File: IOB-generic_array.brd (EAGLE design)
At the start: 106.7 x 104.1 mm, 79 parts

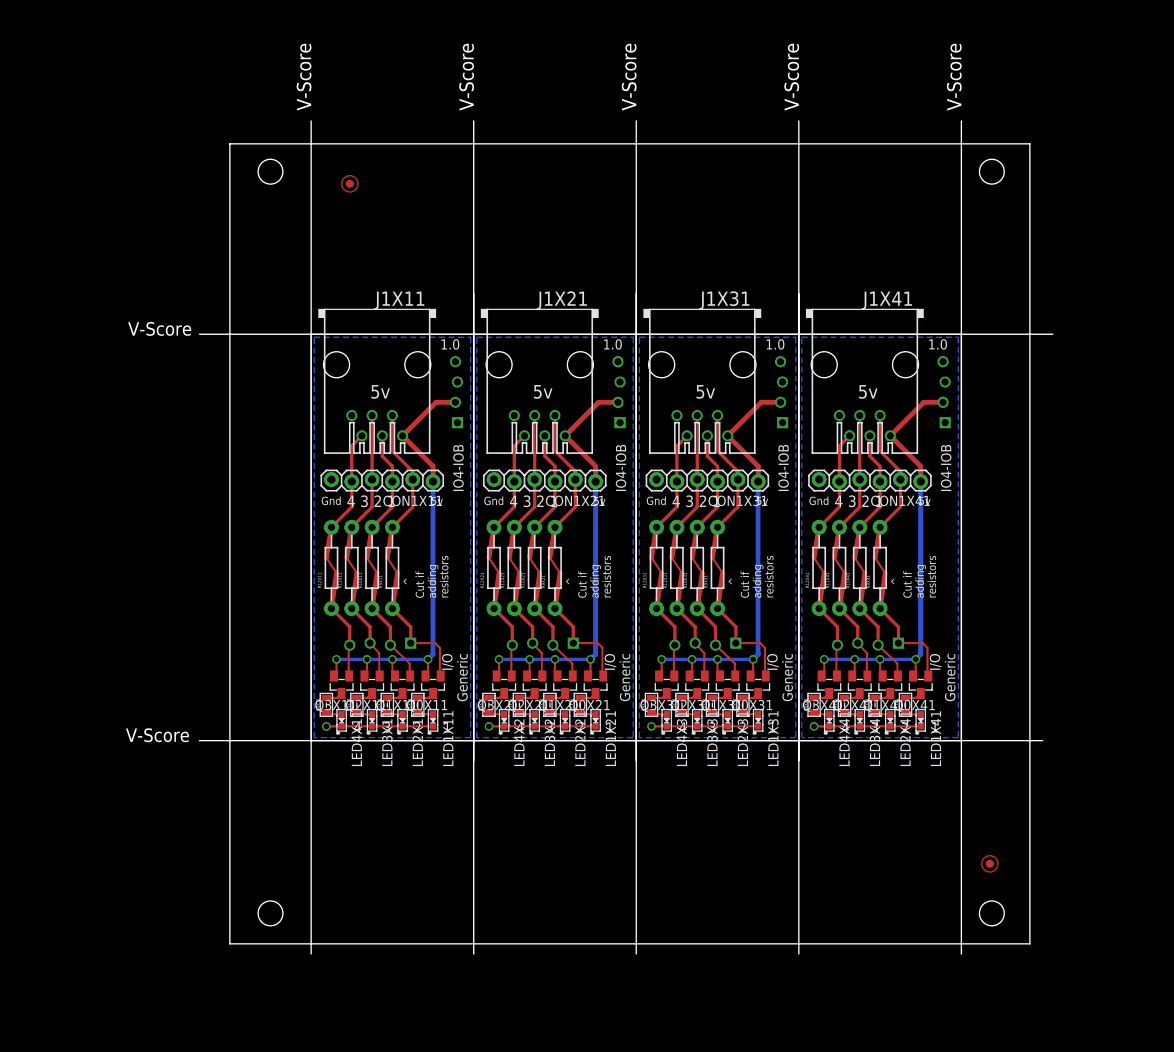
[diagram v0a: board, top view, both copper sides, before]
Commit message: generated new array
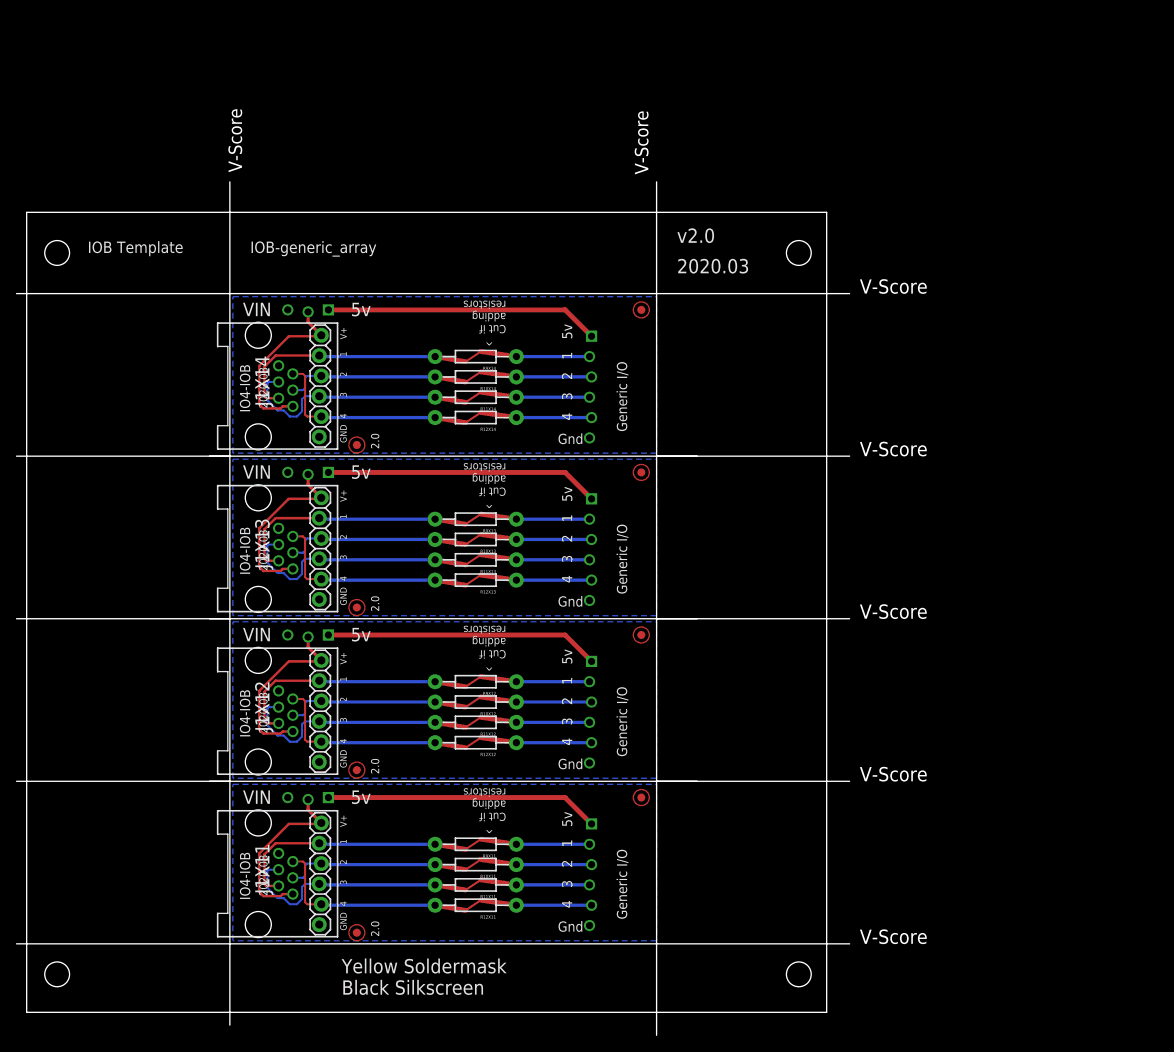
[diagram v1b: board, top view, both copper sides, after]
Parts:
- removed CON1X11, CON1X21, CON1X31, CON1X41: (no value), SPCoast:1X06_LOCK
- removed FID1, FID3: (no value), SPCoast:FIDUCIAL_1MM
- removed IOBX21, IOBX31, IOBX41: (no value), SPCoast:IO4-IOB
- removed J1X21, J1X31, J1X41: (no value), SPCoast:RJ25-PANEL
- removed LED1X11, LED1X21, LED1X31, LED1X41, LED2X11, LED2X21, LED2X31, LED2X41, LED3X11, LED3X21, LED3X31, LED3X41, LED4X11, LED4X21, LED4X31, LED4X41: (no value), SPCoast:0603-LED
- removed Q0X11, Q0X21, Q0X31, Q0X41, Q1X11, Q1X21, Q1X31, Q1X41, Q2X11, Q2X21, Q2X31, Q2X41, Q3X11, Q3X21, Q3X31, Q3X41: (no value), SPCoast:SOT23
- removed R10X21, R10X31, R10X41, R11X21, R11X31, R11X41, R12X21, R12X31, R12X41, R9X21, R9X31, R9X41: (no value), SPCoast:AXIAL-0.4-RES
- removed R1X11, R1X21, R1X31, R1X41, R2X11, R2X21, R2X31, R2X41, R3X11, R3X21, R3X31, R3X41, R4X11, R4X21, R4X31, R4X41: (no value), SPCoast:0805-RES
- removed VINX1: (no value), SPCoast:BOARD-DINRAIL-3.17IN-4X-IOB
- added FID1X11, FID1X12, FID1X13, FID1X14, FID2X11, FID2X12, FID2X13, FID2X14: (no value), SPCoast:FIDUCIAL_1MM
- added IOBX12, IOBX13, IOBX14: (no value), SPCoast:IO4-IOB
- added J1X12, J1X13, J1X14: (no value), SPCoast:RJ24-INVERTED-PINS
- added R10X12, R10X13, R10X14, R11X12, R11X13, R11X14, R12X12, R12X13, R12X14, R9X12, R9X13, R9X14: (no value), SPCoast:AXIAL-0.4-RES
- added R12X1: (no value), SPCoast:BOARD-DINRAIL-3.17IN-H4X-IOB
- J1X11: device SPCoast:RJ25-PANEL -> SPCoast:RJ24-INVERTED-PINS
- moved IOBX11 76.9 mm to (0.00, 0.00), turned to 0 degrees
- moved J1X11 64.6 mm to (7.37, 8.76), turned to 90 degrees
- moved R12X11 45.9 mm to (30.7, 4.83), turned to 180 degrees
- moved R11X11 42.5 mm to (30.7, 7.37), turned to 180 degrees
- moved R10X11 39.3 mm to (30.7, 9.91), turned to 180 degrees
- moved R9X11 36.1 mm to (30.7, 12.4), turned to 180 degrees
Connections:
- removed net !IO1X21: CON1X21.2, J1X21.2, R9X21.P$2
- removed net !IO1X31: CON1X31.2, J1X31.2, R9X31.P$2
- removed net !IO1X41: CON1X41.2, J1X41.2, R9X41.P$2
- removed net !IO2X21: CON1X21.3, J1X21.3, R10X21.P$2
- removed net !IO2X31: CON1X31.3, J1X31.3, R10X31.P$2
- removed net !IO2X41: CON1X41.3, J1X41.3, R10X41.P$2
- removed net !IO3X21: CON1X21.4, J1X21.4, R11X21.P$2
- removed net !IO3X31: CON1X31.4, J1X31.4, R11X31.P$2
- removed net !IO3X41: CON1X41.4, J1X41.4, R11X41.P$2
- removed net !IO4X21: CON1X21.5, J1X21.5, R12X21.P$2
- removed net !IO4X31: CON1X31.5, J1X31.5, R12X31.P$2
- removed net !IO4X41: CON1X41.5, J1X41.5, R12X41.P$2
- removed net GNDX21: CON1X21.6, IOBX21.G@1, IOBX21.G@2, J1X21.6, LED1X21.C, LED2X21.C, LED3X21.C, LED4X21.C
- removed net GNDX31: CON1X31.6, IOBX31.G@1, IOBX31.G@2, J1X31.6, LED1X31.C, LED2X31.C, LED3X31.C, LED4X31.C
- removed net GNDX41: CON1X41.6, IOBX41.G@1, IOBX41.G@2, J1X41.6, LED1X41.C, LED2X41.C, LED3X41.C, LED4X41.C
- removed net N$11X11: Q0X11.3, R1X11.2
- removed net N$11X21: Q0X21.3, R1X21.2
- removed net N$11X31: Q0X31.3, R1X31.2
- removed net N$11X41: Q0X41.3, R1X41.2
- removed net N$2X11: LED1X11.A, R1X11.1
- removed net N$2X21: LED1X21.A, R1X21.1
- removed net N$2X31: LED1X31.A, R1X31.1
- removed net N$2X41: LED1X41.A, R1X41.1
- removed net N$30X11: Q1X11.3, R2X11.2
- removed net N$30X21: Q1X21.3, R2X21.2
- removed net N$30X31: Q1X31.3, R2X31.2
- removed net N$30X41: Q1X41.3, R2X41.2
- removed net N$31X11: Q2X11.3, R3X11.2
- removed net N$31X21: Q2X21.3, R3X21.2
- removed net N$31X31: Q2X31.3, R3X31.2
- removed net N$31X41: Q2X41.3, R3X41.2
- removed net N$32X11: Q3X11.3, R4X11.2
- removed net N$32X21: Q3X21.3, R4X21.2
- removed net N$32X31: Q3X31.3, R4X31.2
- removed net N$32X41: Q3X41.3, R4X41.2
- removed net N$3X11: LED2X11.A, R2X11.1
- removed net N$3X21: LED2X21.A, R2X21.1
- removed net N$3X31: LED2X31.A, R2X31.1
- removed net N$3X41: LED2X41.A, R2X41.1
- removed net N$4X11: LED3X11.A, R3X11.1
- removed net N$4X21: LED3X21.A, R3X21.1
- removed net N$4X31: LED3X31.A, R3X31.1
- removed net N$4X41: LED3X41.A, R3X41.1
- removed net N$5X11: LED4X11.A, R4X11.1
- removed net N$5X21: LED4X21.A, R4X21.1
- removed net N$5X31: LED4X31.A, R4X31.1
- removed net N$5X41: LED4X41.A, R4X41.1
- removed net P1X21: IOBX21.P1, Q0X21.1, R9X21.P$1
- removed net P1X31: IOBX31.P1, Q0X31.1, R9X31.P$1
- removed net P1X41: IOBX41.P1, Q0X41.1, R9X41.P$1
- removed net P2X21: IOBX21.P2, Q1X21.1, R10X21.P$1
- removed net P2X31: IOBX31.P2, Q1X31.1, R10X31.P$1
- removed net P2X41: IOBX41.P2, Q1X41.1, R10X41.P$1
- removed net P3X21: IOBX21.P3, Q2X21.1, R11X21.P$1
- removed net P3X31: IOBX31.P3, Q2X31.1, R11X31.P$1
- removed net P3X41: IOBX41.P3, Q2X41.1, R11X41.P$1
- removed net P4X21: IOBX21.P4, Q3X21.1, R12X21.P$1
- removed net P4X31: IOBX31.P4, Q3X31.1, R12X31.P$1
- removed net P4X41: IOBX41.P4, Q3X41.1, R12X41.P$1
- removed net VCCIOX21: IOBX21.V+
- removed net VCCIOX31: IOBX31.V+
- removed net VCCIOX41: IOBX41.V+
- removed net VCCX21: CON1X21.1, IOBX21.V5, J1X21.1, Q0X21.2, Q1X21.2, Q2X21.2, Q3X21.2
- removed net VCCX31: CON1X31.1, IOBX31.V5, J1X31.1, Q0X31.2, Q1X31.2, Q2X31.2, Q3X31.2
- removed net VCCX41: CON1X41.1, IOBX41.V5, J1X41.1, Q0X41.2, Q1X41.2, Q2X41.2, Q3X41.2
- new net !IO1X12: J1X12.2, J1X12.2@1, R9X12.P$2
- new net !IO1X13: J1X13.2, J1X13.2@1, R9X13.P$2
- new net !IO1X14: J1X14.2, J1X14.2@1, R9X14.P$2
- new net !IO2X12: J1X12.3, J1X12.3@1, R10X12.P$2
- new net !IO2X13: J1X13.3, J1X13.3@1, R10X13.P$2
- new net !IO2X14: J1X14.3, J1X14.3@1, R10X14.P$2
- new net !IO3X12: J1X12.4, J1X12.4@1, R11X12.P$2
- new net !IO3X13: J1X13.4, J1X13.4@1, R11X13.P$2
- new net !IO3X14: J1X14.4, J1X14.4@1, R11X14.P$2
- new net !IO4X12: J1X12.5, J1X12.5@1, R12X12.P$2
- new net !IO4X13: J1X13.5, J1X13.5@1, R12X13.P$2
- new net !IO4X14: J1X14.5, J1X14.5@1, R12X14.P$2
- new net GNDX12: IOBX12.G@3, J1X12.6, J1X12.6@1
- new net GNDX13: IOBX13.G@3, J1X13.6, J1X13.6@1
- new net GNDX14: IOBX14.G@3, J1X14.6, J1X14.6@1
- new net P1X12: IOBX12.P1, R9X12.P$1
- new net P1X13: IOBX13.P1, R9X13.P$1
- new net P1X14: IOBX14.P1, R9X14.P$1
- new net P2X12: IOBX12.P2, R10X12.P$1
- new net P2X13: IOBX13.P2, R10X13.P$1
- new net P2X14: IOBX14.P2, R10X14.P$1
- new net P3X12: IOBX12.P3, R11X12.P$1
- new net P3X13: IOBX13.P3, R11X13.P$1
- new net P3X14: IOBX14.P3, R11X14.P$1
- new net P4X12: IOBX12.P4, R12X12.P$1
- new net P4X13: IOBX13.P4, R12X13.P$1
- new net P4X14: IOBX14.P4, R12X14.P$1
- new net VCCIOX12: IOBX12.V+
- new net VCCIOX13: IOBX13.V+
- new net VCCIOX14: IOBX14.V+
- new net VCCX12: IOBX12.V5, IOBX12.V5@1
- new net VCCX13: IOBX13.V5, IOBX13.V5@1
- new net VCCX14: IOBX14.V5, IOBX14.V5@1
- new net VOUTX11: IOBX11.VOUT, J1X11.1, J1X11.1@1
- new net VOUTX12: IOBX12.VOUT, J1X12.1, J1X12.1@1
- new net VOUTX13: IOBX13.VOUT, J1X13.1, J1X13.1@1
- new net VOUTX14: IOBX14.VOUT, J1X14.1, J1X14.1@1
- net !IO1X11: now also J1X11.2@1; no longer CON1X11.2
- net !IO2X11: now also J1X11.3@1; no longer CON1X11.3
- net !IO3X11: now also J1X11.4@1; no longer CON1X11.4
- net !IO4X11: now also J1X11.5@1; no longer CON1X11.5
- net GNDX11: now also IOBX11.G@3, J1X11.6@1; no longer CON1X11.6, IOBX11.G@1, IOBX11.G@2, LED1X11.C, LED2X11.C, LED3X11.C, LED4X11.C
- net P1X11: no longer Q0X11.1
- net P2X11: no longer Q1X11.1
- net P3X11: no longer Q2X11.1
- net P4X11: no longer Q3X11.1
- net VCCX11: now also IOBX11.V5@1; no longer CON1X11.1, J1X11.1, Q0X11.2, Q1X11.2, Q2X11.2, Q3X11.2
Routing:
- net VCCX31: track 58.7 -> 0.00 mm, vias 4 -> 0
- net VCCX21: track 58.7 -> 0.00 mm, vias 4 -> 0
- net VCCX41: track 58.7 -> 0.00 mm, vias 4 -> 0
- net VCCX14: track 0.00 -> 34.3 mm
- net VCCX13: track 0.00 -> 34.3 mm
- net VCCX12: track 0.00 -> 34.3 mm
- net !IO1X14: track 0.00 -> 33.7 mm, vias 0 -> 1
- net !IO1X13: track 0.00 -> 33.7 mm, vias 0 -> 1
- net !IO1X12: track 0.00 -> 33.7 mm, vias 0 -> 1
- net !IO3X14: track 0.00 -> 33.6 mm, vias 0 -> 1
- net !IO3X13: track 0.00 -> 33.6 mm, vias 0 -> 1
- net !IO3X12: track 0.00 -> 33.6 mm, vias 0 -> 1
- net !IO4X14: track 0.00 -> 29.0 mm, vias 0 -> 1
- net !IO4X12: track 0.00 -> 29.0 mm, vias 0 -> 1
- net !IO4X13: track 0.00 -> 29.0 mm, vias 0 -> 1
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- added copper zone on layer 16, net GNDX12
- added copper zone on layer 16, net GNDX13
- added copper zone on layer 16, net GNDX14
- removed copper zone on layer 16, net GNDX21
- removed copper zone on layer 16, net GNDX31
- removed copper zone on layer 16, net GNDX41
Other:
- board size 106.7 x 104.1 mm -> 104.1 x 106.7 mm
- board text added: "2.0"
- board text added: "2020.03"
- board text added: "Generic I/O"
- board text added: "Generic Quad I/O"
- board text added: "v2.0"
- board text removed: "1"
- board text removed: "1.0"
- board text removed: "15, 95"
- board text removed: "2"
- board text removed: "3"
- board text removed: "4"
- board text removed: "4 3 2 1"
- board text removed: "5v"
- board text removed: "95, 10"
- board text removed: "Gnd"
- board text removed: "I/O Generic"
- board text removed: "IOB I/O Generic"
- board text removed: "IOB to IO4 Interface"
- board text removed: "Made in the PCR, Coast Div, NMRA"
- board text removed: "Model Railroading is Fun!"
- board text removed: "Q0"
- board text removed: "Q1"
- board text removed: "Q2"
- board text removed: "Q3"
- board text removed: "Quad I/O"
- board text removed: "R1"
- board text removed: "R10"
- board text removed: "R11"
- board text removed: "R12"
- board text removed: "R2"
- board text removed: "R3"
- board text removed: "R4"
- board text removed: "R9"
- board text removed: "SPCoast.com John Plocher"
- board text removed: "V1.0 2020-01"

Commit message: added array...
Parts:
- moved R12X1 26.9 mm to (0.00, 0.00)
- moved FID1X11 26.8 mm to (41.3, 9.96)
- moved FID1X12 26.8 mm to (41.3, 30.3)
- moved FID1X13 26.8 mm to (41.3, 50.6)
- moved FID1X14 26.8 mm to (41.3, 70.9)
- moved IOBX11 26.8 mm to (25.4, 8.56)
- moved IOBX12 26.8 mm to (25.4, 28.9)
- moved IOBX13 26.8 mm to (25.4, 49.2)
- moved J1X11 26.8 mm to (32.8, 17.3)
- moved J1X12 26.8 mm to (32.8, 37.6)
- moved J1X13 26.8 mm to (32.8, 58.0)
- moved J1X14 26.8 mm to (32.8, 78.3)
- moved R10X11 26.8 mm to (56.1, 18.5)
- moved R10X12 26.8 mm to (56.1, 38.8)
- moved R10X13 26.8 mm to (56.1, 59.1)
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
